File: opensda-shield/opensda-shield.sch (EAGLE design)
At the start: 13 parts, among them IC1 74HC125D, IC2 74HC125N, J1 61302011121, J2 61302011121, J3 61300211121, J4 CORTEX_DEBUG_PTH, J5 61301511121

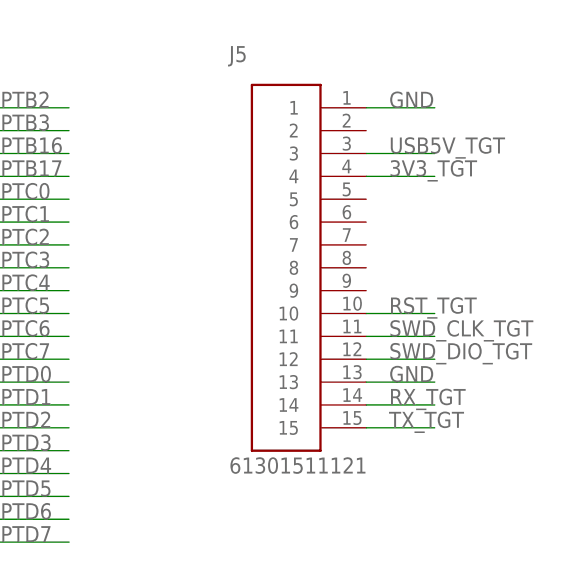
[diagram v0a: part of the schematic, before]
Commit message: Pridana dalsi GND na 15pinovy konektor
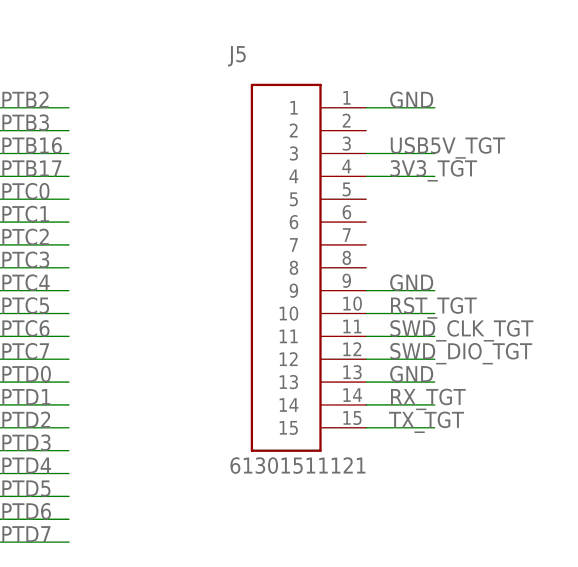
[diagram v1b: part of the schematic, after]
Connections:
- net GND: now also J5.9
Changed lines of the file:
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@@
 <label x="205.74" y="25.4" size="1.778" layer="95"/>
+</segment>
+<segment>
+<pinref part="J5" gate="G$1" pin="9"/>
+<wire x1="261.62" y1="76.2" x2="269.24" y2="76.2" width="0.1524" layer="91"/>
+<label x="264.16" y="76.2" size="1.778" layer="95"/>
 </segment>
 </net>

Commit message: Zmeny podle e-mailu
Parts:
- added J6, J7: 61300211121, Headers:61300211121
- added R6: 10k, rcl:R-EU_R0805
- IC1: value 74HC125D -> 74LVC125
- IC2: value 74HC125N -> 74LVC125
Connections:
- removed net USB5V_TGT: J5.3
- new net N$1: J5.3, J6.2
- new net N$4: J5.4, J7.1
- new net N$5: IC2C.I, IC2C.OE, IC2D.I, IC2D.OE, R6.1
- net 3V3: now also J7.2, R6.2
- net 3V3_TGT: no longer J5.4
- net GND: now also IC2B.OE
- net TX_TGT: no longer IC2C.OE
- net USB5V: now also J6.1
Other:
- moved on the sheet: IC1P, IC2C, IC2D, IC2P, J1, J2, J3, J4, J5, LED1, R1, R2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

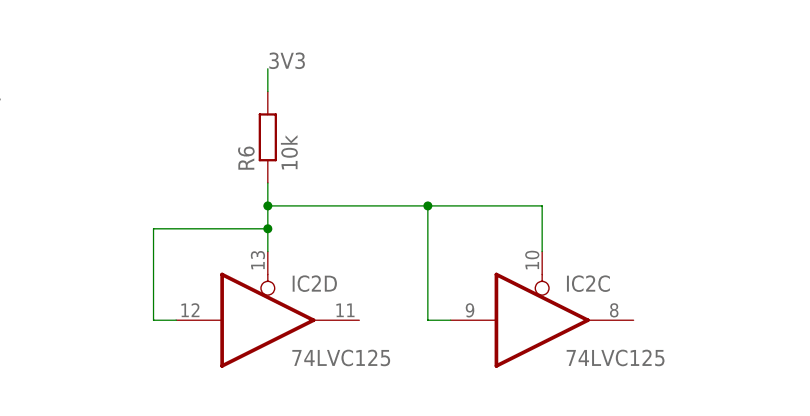
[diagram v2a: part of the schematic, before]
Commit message: Zmena 74LVC125 package z SO14 na TSSOP14
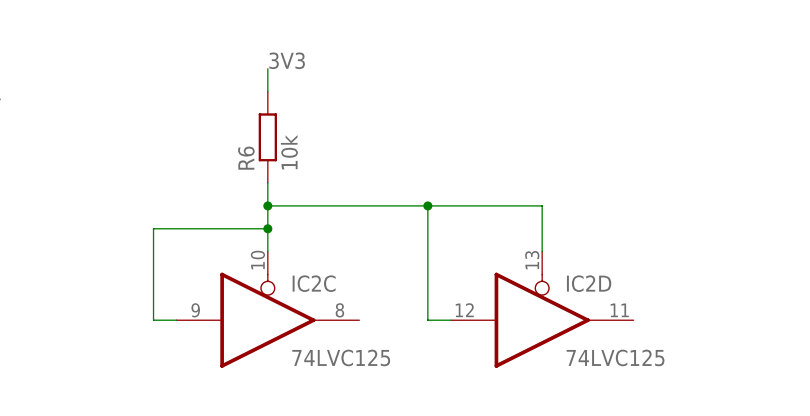
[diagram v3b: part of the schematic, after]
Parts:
- IC1: device 74xx-eu:74HC125D -> 74xx-eu:74ABT125PW
- IC2: device 74xx-eu:74HC125N -> 74xx-eu:74ABT125PW
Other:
- moved on the sheet: IC2C, IC2D

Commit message: Prvni verze shieldu
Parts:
- removed J6, J7: 61300211121, Headers:61300211121
- added C1, C2: 0.1uF, rcl:C-EUC0805
- added JP1: (no value), pinhead:PINHD-2X2
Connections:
- removed net N$4: J5.4, J7.1
- new net N$3: J5.4, JP1.1
- net 3V3: now also C1.2, C2.1, JP1.2; no longer J7.2
- net GND: now also C1.1, C2.2
- net N$1: now also JP1.3; no longer J6.2
- net USB5V: now also JP1.4; no longer J6.1

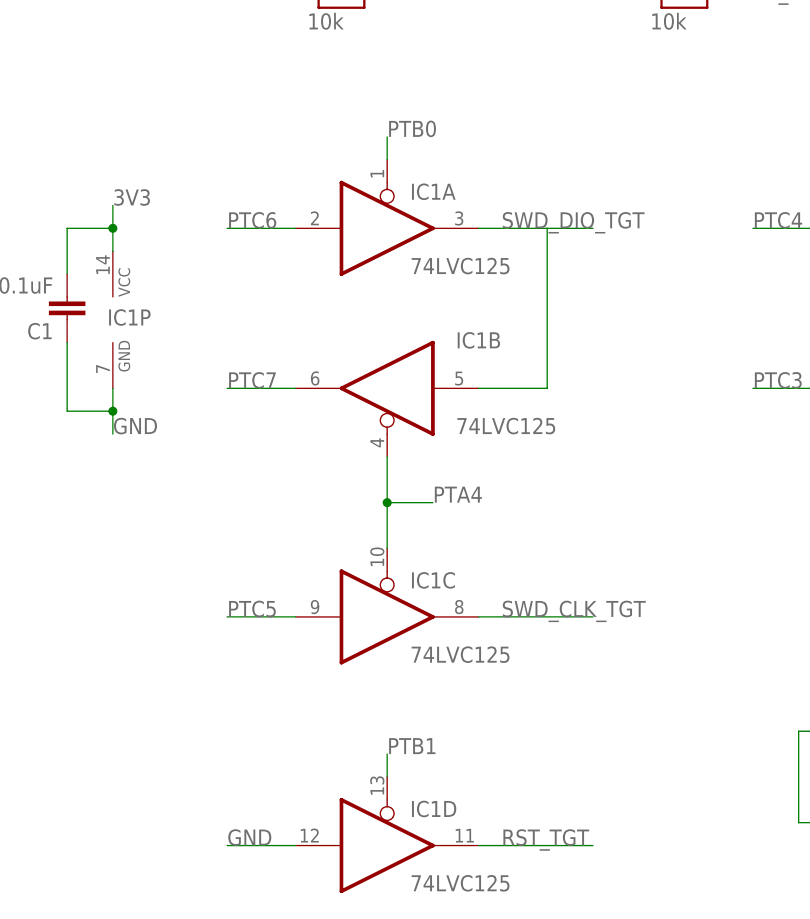
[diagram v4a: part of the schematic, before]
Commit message: Premisten J4 a prehozeny gaty bufferu
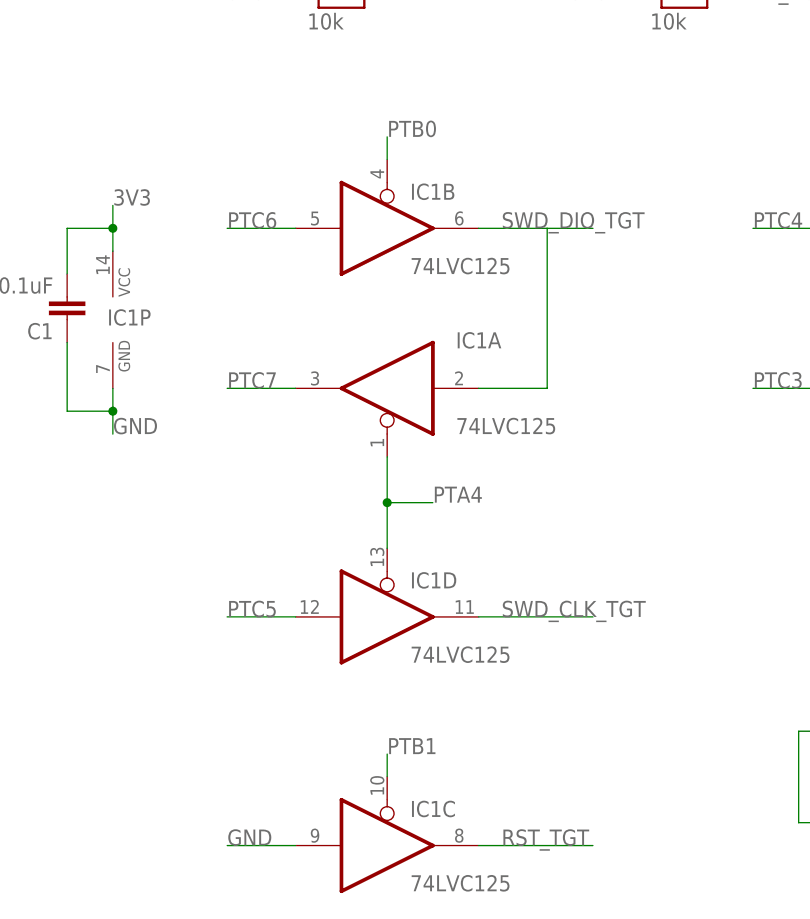
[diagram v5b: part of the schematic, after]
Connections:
- net GND: now also IC1C.I; no longer IC1D.I
- net PTA4: now also IC1A.OE, IC1D.OE; no longer IC1B.OE, IC1C.OE
- net PTB0: now also IC1B.OE; no longer IC1A.OE
- net PTB1: now also IC1C.OE; no longer IC1D.OE
- net PTC5: now also IC1D.I; no longer IC1C.I
- net PTC6: now also IC1B.I; no longer IC1A.I
- net PTC7: now also IC1A.O; no longer IC1B.O
- net RST_TGT: now also IC1C.O; no longer IC1D.O
- net SWD_CLK_TGT: now also IC1D.O; no longer IC1C.O
- net SWD_DIO_TGT: now also IC1A.I, IC1B.O; no longer IC1A.O, IC1B.I
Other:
- moved on the sheet: IC1A, IC1B, IC1C, IC1D
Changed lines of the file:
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@@
 <attribute name="VALUE" x="104.902" y="36.83" size="1.778" layer="96" rot="R90"/>
 </instance>
-<instance part="IC1" gate="A" x="43.18" y="86.36" smashed="yes">
+<instance part="IC1" gate="B" x="43.18" y="86.36" smashed="yes">
 <attribute name="NAME" x="45.72" y="89.535" size="1.778" layer="95"/>
 <attribute name="VALUE" x="45.72" y="81.28" size="1.778" layer="96"/>
 </instance>
-<instance part="IC1" gate="B" x="43.18" y="68.58" smashed="yes" rot="R180">
+<instance part="IC1" gate="A" x="43.18" y="68.58" smashed="yes" rot="R180">
 <attribute name="NAME" x="50.8" y="73.025" size="1.778" layer="95"/>
 <attribute name="VALUE" x="50.8" y="63.5" size="1.778" layer="96"/>
 </instance>
-<instance part="IC1" gate="C" x="43.18" y="43.18" smashed="yes">
+<instance part="IC1" gate="D" x="43.18" y="43.18" smashed="yes">
 <attribute name="NAME" x="45.72" y="46.355" size="1.778" layer="95"/>
 <attribute name="VALUE" x="45.72" y="38.1" size="1.778" layer="96"/>
 </instance>
-<instance part="IC1" gate="D" x="43.18" y="17.78" smashed="yes">
+<instance part="IC1" gate="C" x="43.18" y="17.78" smashed="yes">
 <attribute name="NAME" x="45.72" y="20.955" size="1.778" layer="95"/>
 <attribute name="VALUE" x="45.72" y="12.7" size="1.778" layer="96"/>
@@
 <wire x1="33.02" y1="17.78" x2="25.4" y2="17.78" width="0.1524" layer="91"/>
 <label x="25.4" y="17.78" size="1.778" layer="95"/>
-<pinref part="IC1" gate="D" pin="I"/>
+<pinref part="IC1" gate="C" pin="I"/>
 </segment>
 <segment>
@@
 <wire x1="43.18" y1="55.88" x2="48.26" y2="55.88" width="0.1524" layer="91"/>
 <junction x="43.18" y="55.88"/>
-<pinref part="IC1" gate="B" pin="OE"/>
-<pinref part="IC1" gate="C" pin="OE"/>
+<pinref part="IC1" gate="A" pin="OE"/>
+<pinref part="IC1" gate="D" pin="OE"/>
 </segment>
 </net>
@@
 <wire x1="43.18" y1="93.98" x2="43.18" y2="96.52" width="0.1524" layer="91"/>
 <label x="43.18" y="96.52" size="1.778" layer="95"/>
-<pinref part="IC1" gate="A" pin="OE"/>
+<pinref part="IC1" gate="B" pin="OE"/>
 </segment>
 <segment>
@@
 <wire x1="43.18" y1="25.4" x2="43.18" y2="27.94" width="0.1524" layer="91"/>
 <label x="43.18" y="27.94" size="1.778" layer="95"/>
-<pinref part="IC1" gate="D" pin="OE"/>
+<pinref part="IC1" gate="C" pin="OE"/>
 </segment>
 <segment>
@@
 <wire x1="33.02" y1="43.18" x2="25.4" y2="43.18" width="0.1524" layer="91"/>
 <label x="25.4" y="43.18" size="1.778" layer="95"/>
-<pinref part="IC1" gate="C" pin="I"/>
+<pinref part="IC1" gate="D" pin="I"/>
 </segment>
 </net>
@@
 <wire x1="33.02" y1="86.36" x2="25.4" y2="86.36" width="0.1524" layer="91"/>
 <label x="25.4" y="86.36" size="1.778" layer="95"/>
-<pinref part="IC1" gate="A" pin="I"/>
+<pinref part="IC1" gate="B" pin="I"/>
 </segment>
 </net>
@@
 <wire x1="33.02" y1="68.58" x2="25.4" y2="68.58" width="0.1524" layer="91"/>
 <label x="25.4" y="68.58" size="1.778" layer="95"/>
-<pinref part="IC1" gate="B" pin="O"/>
+<pinref part="IC1" gate="A" pin="O"/>
 </segment>
 </net>
@@
 <wire x1="53.34" y1="68.58" x2="60.96" y2="68.58" width="0.1524" layer="91"/>
 <wire x1="60.96" y1="68.58" x2="60.96" y2="86.36" width="0.1524" layer="91"/>
-<pinref part="IC1" gate="A" pin="O"/>
-<pinref part="IC1" gate="B" pin="I"/>
+<pinref part="IC1" gate="B" pin="O"/>
+<pinref part="IC1" gate="A" pin="I"/>
 </segment>
 <segment>
@@
 <wire x1="53.34" y1="43.18" x2="66.04" y2="43.18" width="0.1524" layer="91"/>
 <label x="55.88" y="43.18" size="1.778" layer="95"/>
-<pinref part="IC1" gate="C" pin="O"/>
+<pinref part="IC1" gate="D" pin="O"/>
 </segment>
 <segment>
@@
 <wire x1="53.34" y1="17.78" x2="66.04" y2="17.78" width="0.1524" layer="91"/>
 <label x="55.88" y="17.78" size="1.778" layer="95"/>
-<pinref part="IC1" gate="D" pin="O"/>
-</segment>
-<segment>
+<pinref part="IC1" gate="C" pin="O"/>
+</segment>
+<segment>

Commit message: Zmeny z e-mailu
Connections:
- net N$1 renamed 3V3_OUT
- net N$3 renamed USB5V_OUT
- net PTA4 renamed !SDA_SWD_EN_PTA4
- net PTB0 renamed !SDA_SWD_OE_PTB0
- net PTB1 renamed !SDA_RST_TGTMCU_PTB1
- net PTC3 renamed UART0_TX_TGTMCU_PTC3
- net PTC4 renamed UART0_RX_TGTMCU_PTC4
- net PTC5 renamed SDA_SPI0_SCK_PTC5
- net PTC6 renamed SDA_SPI0_SOUT_PTC6
- net PTC7 renamed SDA_SPI0_SIN_PTC7
- net PTD4 renamed !SDA_LED_PTD4
- net RST_TGT renamed !RST_TGT
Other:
- moved on the sheet: C1, C2, IC1A, IC1B, IC1C, IC1D, IC1P, IC2A, IC2B, IC2C, IC2D, IC2P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

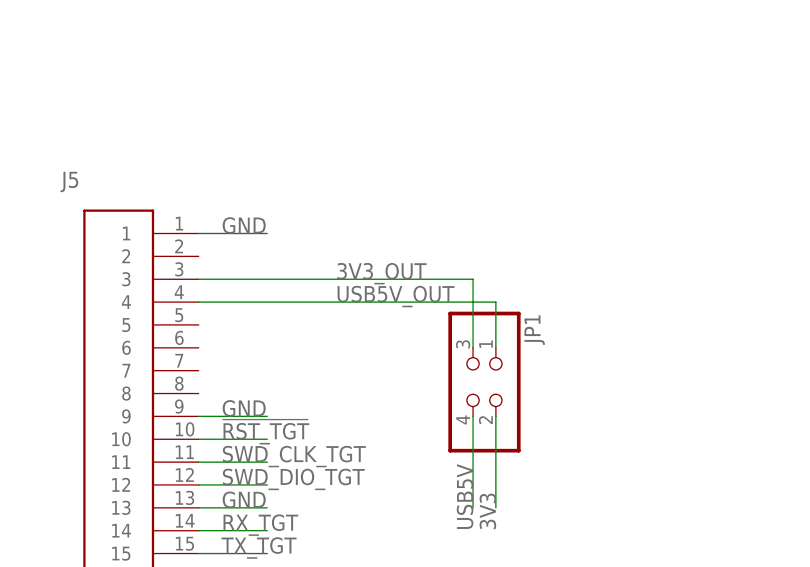
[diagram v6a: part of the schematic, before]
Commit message: Zmeny popisku
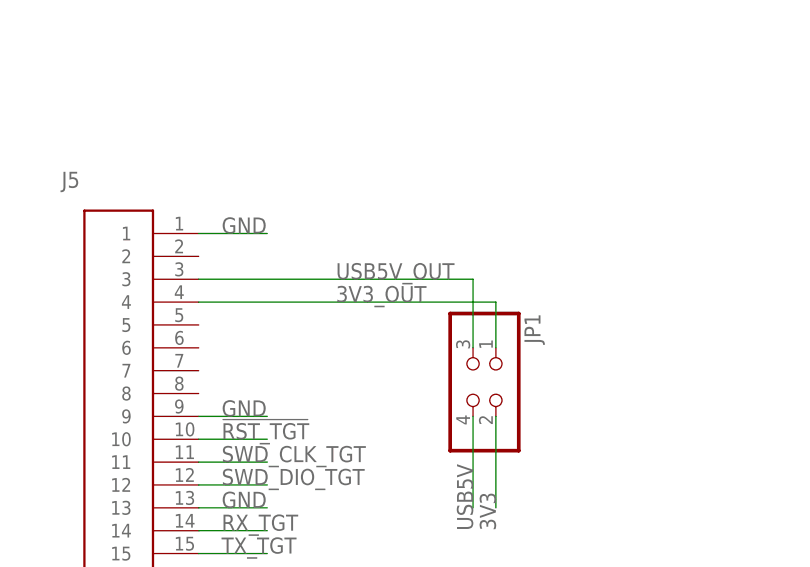
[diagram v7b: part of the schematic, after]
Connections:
- net 3V3_OUT: now also J5.4, JP1.1; no longer J5.3, JP1.3
- net USB5V_OUT: now also J5.3, JP1.3; no longer J5.4, JP1.1
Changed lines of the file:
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@@
 <net name="3V3_OUT" class="0">
+<segment>
+<pinref part="J5" gate="G$1" pin="4"/>
+<wire x1="220.98" y1="60.96" x2="254" y2="60.96" width="0.1524" layer="91"/>
+<pinref part="JP1" gate="A" pin="1"/>
+<wire x1="254" y1="60.96" x2="254" y2="55.88" width="0.1524" layer="91"/>
+<label x="236.22" y="60.96" size="1.778" layer="95"/>
+</segment>
+</net>
+<net name="USB5V_OUT" class="0">
 <segment>
 <pinref part="J5" gate="G$1" pin="3"/>
@@
 </segment>
 </net>
-<net name="USB5V_OUT" class="0">
-<segment>
-<pinref part="J5" gate="G$1" pin="4"/>
-<wire x1="220.98" y1="60.96" x2="254" y2="60.96" width="0.1524" layer="91"/>
-<pinref part="JP1" gate="A" pin="1"/>
-<wire x1="254" y1="60.96" x2="254" y2="55.88" width="0.1524" layer="91"/>
-<label x="236.22" y="60.96" size="1.778" layer="95"/>
-</segment>
-</net>

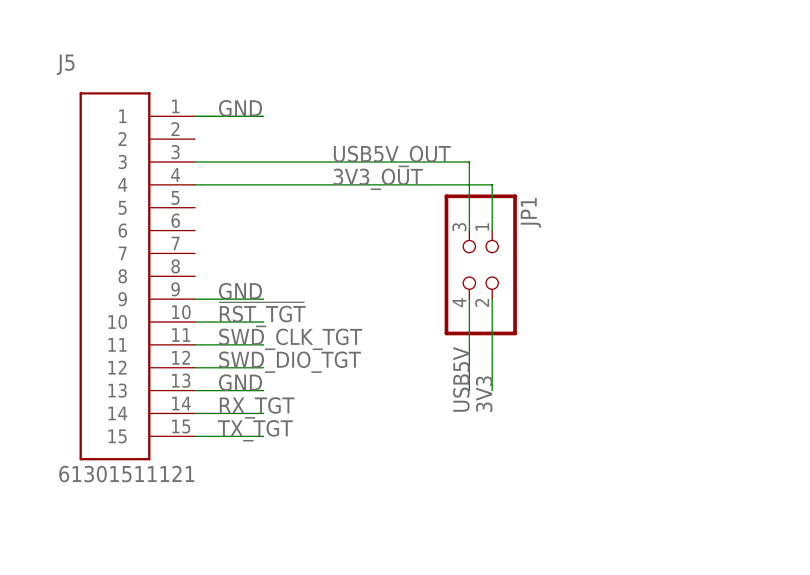
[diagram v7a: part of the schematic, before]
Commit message: Posunuti 10pin konektoru a zmena 2x2 jumperu na 3x2
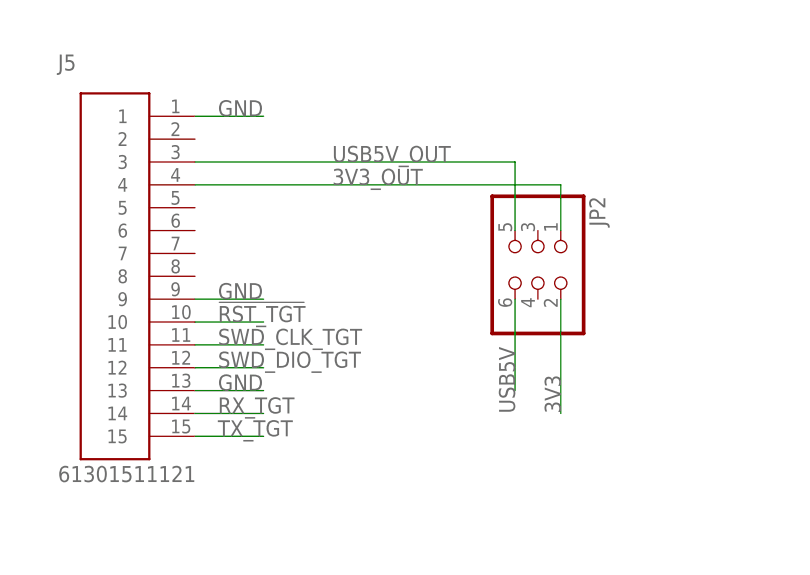
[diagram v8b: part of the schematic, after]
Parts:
- removed JP1: (no value), pinhead:PINHD-2X2
- added JP2: (no value), pinhead:PINHD-2X3
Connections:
- net 3V3: now also JP2.2; no longer JP1.2
- net 3V3_OUT: now also JP2.1; no longer JP1.1
- net USB5V: now also JP2.6; no longer JP1.4
- net USB5V_OUT: now also JP2.5; no longer JP1.3
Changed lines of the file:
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@@
 <part name="IC1" library="74xx-eu" library_urn="urn:adsk.eagle:library:85" deviceset="74*125" device="PW" package3d_urn="urn:adsk.eagle:package:2019/3" technology="ABT" value="74LVC125"/>
 <part name="IC2" library="74xx-eu" library_urn="urn:adsk.eagle:library:85" deviceset="74*125" device="PW" package3d_urn="urn:adsk.eagle:package:2019/3" technology="ABT" value="74LVC125"/>
-<part name="JP1" library="pinhead" library_urn="urn:adsk.eagle:library:325" deviceset="PINHD-2X2" device="" package3d_urn="urn:adsk.eagle:package:22455/2"/>
 <part name="C1" library="rcl" library_urn="urn:adsk.eagle:library:334" deviceset="C-EU" device="C0805" package3d_urn="urn:adsk.eagle:package:23617/2" value="0.1uF"/>
 <part name="C2" library="rcl" library_urn="urn:adsk.eagle:library:334" deviceset="C-EU" device="C0805" package3d_urn="urn:adsk.eagle:package:23617/2" value="0.1uF"/>
+<part name="JP2" library="pinhead" library_urn="urn:adsk.eagle:library:325" deviceset="PINHD-2X3" device="" package3d_urn="urn:adsk.eagle:package:22462/2"/>
 </parts>
 <sheets>
@@
 <attribute name="NAME" x="169.545" y="103.505" size="1.778" layer="95"/>
 </instance>
-<instance part="JP1" gate="A" x="251.46" y="50.8" smashed="yes" rot="R270">
-<attribute name="NAME" x="257.175" y="59.69" size="1.778" layer="95" rot="R270"/>
-<attribute name="VALUE" x="246.38" y="59.69" size="1.778" layer="96" rot="R270"/>
-</instance>
 <instance part="C1" gate="G$1" x="10.16" y="137.16" smashed="yes" rot="R180">
 <attribute name="NAME" x="8.636" y="136.779" size="1.778" layer="95" rot="R180"/>
@@
 <attribute name="NAME" x="181.864" y="107.061" size="1.778" layer="95"/>
 <attribute name="VALUE" x="181.864" y="101.981" size="1.778" layer="96"/>
+</instance>
+<instance part="JP2" gate="A" x="259.08" y="53.34" smashed="yes" rot="R270">
+<attribute name="NAME" x="264.795" y="59.69" size="1.778" layer="95" rot="R270"/>
+<attribute name="VALUE" x="251.46" y="59.69" size="1.778" layer="96" rot="R270"/>
 </instance>
 </instances>
@@
 </segment>
 <segment>
-<pinref part="JP1" gate="A" pin="4"/>
-<wire x1="251.46" y1="48.26" x2="251.46" y2="38.1" width="0.1524" layer="91"/>
-<label x="251.46" y="35.56" size="1.778" layer="95" rot="R90"/>
+<wire x1="256.54" y1="48.26" x2="256.54" y2="38.1" width="0.1524" layer="91"/>
+<label x="256.54" y="35.56" size="1.778" layer="95" rot="R90"/>
+<pinref part="JP2" gate="A" pin="6"/>
 </segment>
 </net>
@@
 </segment>
 <segment>
-<pinref part="JP1" gate="A" pin="2"/>
-<wire x1="254" y1="48.26" x2="254" y2="38.1" width="0.1524" layer="91"/>
-<label x="254" y="35.56" size="1.778" layer="95" rot="R90"/>
+<wire x1="261.62" y1="48.26" x2="261.62" y2="35.56" width="0.1524" layer="91"/>
+<label x="261.62" y="35.56" size="1.778" layer="95" rot="R90"/>
+<pinref part="JP2" gate="A" pin="2"/>
 </segment>
 </net>
@@
 <segment>
 <pinref part="J5" gate="G$1" pin="4"/>
-<wire x1="220.98" y1="60.96" x2="254" y2="60.96" width="0.1524" layer="91"/>
-<pinref part="JP1" gate="A" pin="1"/>
-<wire x1="254" y1="60.96" x2="254" y2="55.88" width="0.1524" layer="91"/>
+<wire x1="220.98" y1="60.96" x2="261.62" y2="60.96" width="0.1524" layer="91"/>
+<wire x1="261.62" y1="60.96" x2="261.62" y2="55.88" width="0.1524" layer="91"/>
 <label x="236.22" y="60.96" size="1.778" layer="95"/>
+<pinref part="JP2" gate="A" pin="1"/>
 </segment>
 </net>
@@
 <segment>
 <pinref part="J5" gate="G$1" pin="3"/>
-<pinref part="JP1" gate="A" pin="3"/>
-<wire x1="220.98" y1="63.5" x2="251.46" y2="63.5" width="0.1524" layer="91"/>
-<wire x1="251.46" y1="63.5" x2="251.46" y2="55.88" width="0.1524" layer="91"/>
+<wire x1="220.98" y1="63.5" x2="256.54" y2="63.5" width="0.1524" layer="91"/>
+<wire x1="256.54" y1="63.5" x2="256.54" y2="55.88" width="0.1524" layer="91"/>
 <label x="236.22" y="63.5" size="1.778" layer="95"/>
-</segment>
-</net>
+<pinref part="JP2" gate="A" pin="5"/>
+</segment>
+</net>
